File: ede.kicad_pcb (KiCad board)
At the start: 4 copper layers, 72.1 x 49 mm, 114 parts, among them J1 Conn_01x01, J10 Conn_01x01, J11 Conn_01x01, J12 Conn_01x01, J2 Conn_01x01, J3 Conn_01x01, J4 Conn_01x01, J5 Conn_01x06, J6 Conn_01x01, J7 Conn_01x04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

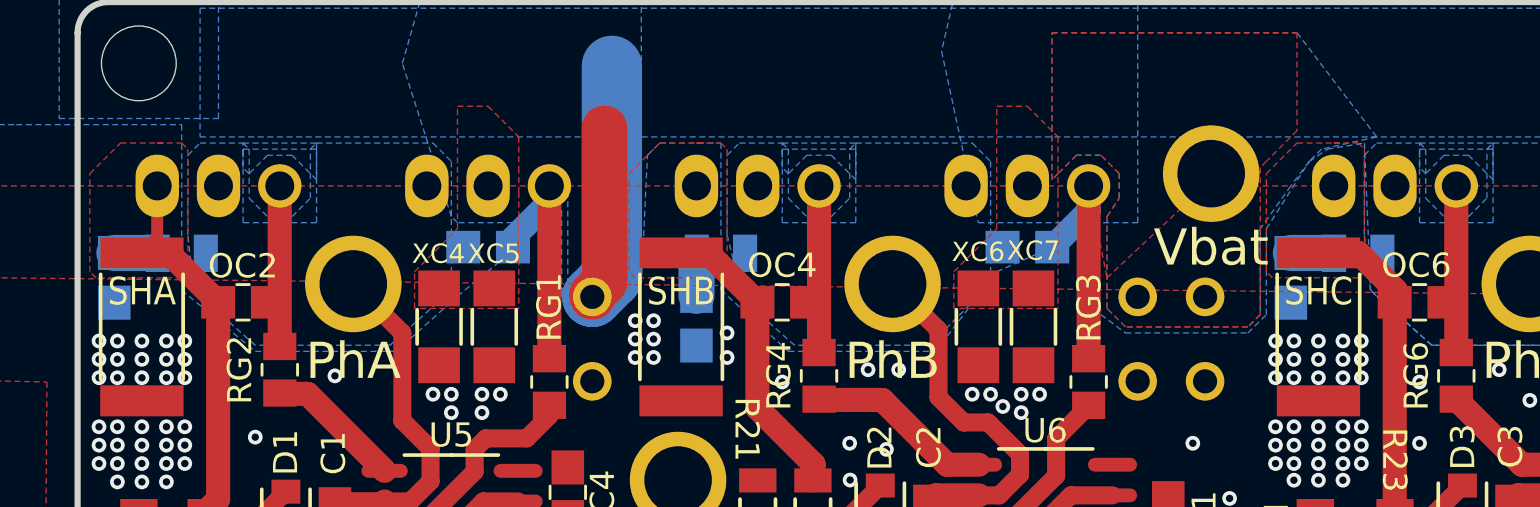
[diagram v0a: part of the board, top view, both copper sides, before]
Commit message: pcb: alter R0805 footprints on B.Cu as per reference
Signed-off-by: Afzal <afzal@intible.in>
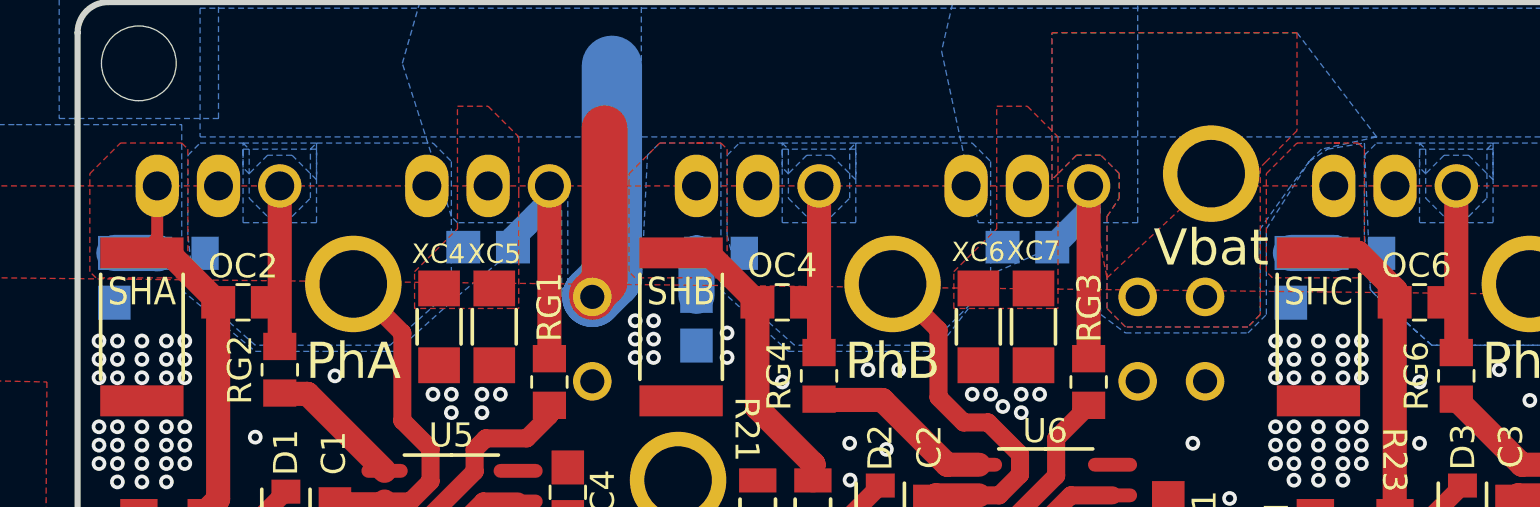
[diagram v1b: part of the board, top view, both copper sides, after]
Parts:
- RS1, RS2, RS3: footprint Intible:R_0805_2012Metric_EDE -> Intible:R_0805_2012Metric_small_EDE
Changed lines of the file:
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@@
     )
   )
-  (footprint "Intible:R_0805_2012Metric_EDE" locked (layer "B.Cu")
+  (footprint "Intible:R_0805_2012Metric_small_EDE" locked (layer "B.Cu")
     (at 97.5868 78.8416)
     (descr "Resistor SMD 0805 (2012 Metric), square (rectangular) end terminal, IPC_7351 nominal, (Body size source: IPC-SM-782 page 72, https://www.pcb-3d.com/wordpress/wp-content/uploads/ipc-sm-782a_amendment_1_and_2.pdf), generated with kicad-footprint-generator")
@@
     (property "exclude_from_bom" "")
     (attr smd exclude_from_bom)
-    (fp_text reference "RS3" (at 2.413 0.5334 90 unlocked) (layer "B.SilkS")
+    (fp_text reference "RS3" (at 2.413 0.5334 90) (layer "B.SilkS")
       (effects (font (size 1 1) (thickness 0.152)) (justify mirror))
     )
@@
       (effects (font (size 0.5 0.5) (thickness 0.08)) (justify mirror))
     )
-    (fp_line (start -0.227064 -0.735) (end 0.227064 -0.735) (layer "B.SilkS") (width 0.152))
-    (fp_line (start -0.227064 0.735) (end 0.227064 0.735) (layer "B.SilkS") (width 0.152))
-    (fp_line (start 1.68 0.95) (end 1.68 -0.95) (layer "B.CrtYd") (width 0.05))
+    (fp_line (start -0.227064 -0.735) (end 0.227064 -0.735) (layer "B.SilkS") (width 0.12))
+    (fp_line (start -0.227064 0.735) (end 0.227064 0.735) (layer "B.SilkS") (width 0.12))
     (fp_line (start -1.68 0.95) (end 1.68 0.95) (layer "B.CrtYd") (width 0.05))
     (fp_line (start 1.68 -0.95) (end -1.68 -0.95) (layer "B.CrtYd") (width 0.05))
     (fp_line (start -1.68 -0.95) (end -1.68 0.95) (layer "B.CrtYd") (width 0.05))
+    (fp_line (start 1.68 0.95) (end 1.68 -0.95) (layer "B.CrtYd") (width 0.05))
+    (fp_line (start 1 -0.625) (end -1 -0.625) (layer "B.Fab") (width 0.1))
+    (fp_line (start -1 -0.625) (end -1 0.625) (layer "B.Fab") (width 0.1))
+    (fp_line (start -1 0.625) (end 1 0.625) (layer "B.Fab") (width 0.1))
     (fp_line (start 1 0.625) (end 1 -0.625) (layer "B.Fab") (width 0.1))
-    (fp_line (start -1 -0.625) (end -1 0.625) (layer "B.Fab") (width 0.1))
-    (fp_line (start 1 -0.625) (end -1 -0.625) (layer "B.Fab") (width 0.1))
-    (fp_line (start -1 0.625) (end 1 0.625) (layer "B.Fab") (width 0.1))
-    (pad "1" smd rect locked (at -1 0) (size 1 1.55) (layers "B.Cu" "B.Paste" "B.Mask")
+    (pad "1" smd rect locked (at -0.9665 0) (size 1.133 1.377) (layers "B.Cu" "B.Paste" "B.Mask")
       (net 12 "Net-(CS3-Pad1)") (pintype "passive"))
-    (pad "2" smd rect locked (at 1 0) (size 1 1.55) (layers "B.Cu" "B.Paste" "B.Mask")
+    (pad "2" smd rect locked (at 0.9665 0) (size 1.133 1.377) (layers "B.Cu" "B.Paste" "B.Mask")
       (net 10 "/PHASEC") (pintype "passive"))
     (model "${KICAD6_3DMODEL_DIR}/Resistor_SMD.3dshapes/R_0805_2012Metric.wrl"
@@
     )
   )
-  (footprint "Intible:R_0805_2012Metric_EDE" locked (layer "B.Cu")
+  (footprint "Intible:R_0805_2012Metric_small_EDE" locked (layer "B.Cu")
     (at 71.1708 78.8416)
     (descr "Resistor SMD 0805 (2012 Metric), square (rectangular) end terminal, IPC_7351 nominal, (Body size source: IPC-SM-782 page 72, https://www.pcb-3d.com/wordpress/wp-content/uploads/ipc-sm-782a_amendment_1_and_2.pdf), generated with kicad-footprint-generator")
@@
     (property "exclude_from_bom" "")
     (attr smd exclude_from_bom)
-    (fp_text reference "RS2" (at 2.3622 0.4064 90 unlocked) (layer "B.SilkS")
+    (fp_text reference "RS2" (at 2.3622 0.4064 90) (layer "B.SilkS")
       (effects (font (size 1 1) (thickness 0.152)) (justify mirror))
     )
@@
       (effects (font (size 0.5 0.5) (thickness 0.08)) (justify mirror))
     )
-    (fp_line (start -0.227064 0.735) (end 0.227064 0.735) (layer "B.SilkS") (width 0.152))
-    (fp_line (start -0.227064 -0.735) (end 0.227064 -0.735) (layer "B.SilkS") (width 0.152))
+    (fp_line (start -0.227064 0.735) (end 0.227064 0.735) (layer "B.SilkS") (width 0.12))
+    (fp_line (start -0.227064 -0.735) (end 0.227064 -0.735) (layer "B.SilkS") (width 0.12))
+    (fp_line (start -1.68 0.95) (end 1.68 0.95) (layer "B.CrtYd") (width 0.05))
     (fp_line (start -1.68 -0.95) (end -1.68 0.95) (layer "B.CrtYd") (width 0.05))
-    (fp_line (start -1.68 0.95) (end 1.68 0.95) (layer "B.CrtYd") (width 0.05))
     (fp_line (start 1.68 -0.95) (end -1.68 -0.95) (layer "B.CrtYd") (width 0.05))
     (fp_line (start 1.68 0.95) (end 1.68 -0.95) (layer "B.CrtYd") (width 0.05))
+    (fp_line (start -1 -0.625) (end -1 0.625) (layer "B.Fab") (width 0.1))
+    (fp_line (start 1 -0.625) (end -1 -0.625) (layer "B.Fab") (width 0.1))
+    (fp_line (start 1 0.625) (end 1 -0.625) (layer "B.Fab") (width 0.1))
     (fp_line (start -1 0.625) (end 1 0.625) (layer "B.Fab") (width 0.1))
-    (fp_line (start -1 -0.625) (end -1 0.625) (layer "B.Fab") (width 0.1))
-    (fp_line (start 1 0.625) (end 1 -0.625) (layer "B.Fab") (width 0.1))
-    (fp_line (start 1 -0.625) (end -1 -0.625) (layer "B.Fab") (width 0.1))
-    (pad "1" smd rect locked (at -1 0) (size 1 1.55) (layers "B.Cu" "B.Paste" "B.Mask")
+    (pad "1" smd rect locked (at -0.9665 0) (size 1.133 1.377) (layers "B.Cu" "B.Paste" "B.Mask")
       (net 11 "Net-(CS2-Pad1)") (pintype "passive"))
-    (pad "2" smd rect locked (at 1 0) (size 1 1.55) (layers "B.Cu" "B.Paste" "B.Mask")
+    (pad "2" smd rect locked (at 0.9665 0) (size 1.133 1.377) (layers "B.Cu" "B.Paste" "B.Mask")
       (net 3 "/PHASEB") (pintype "passive"))
     (model "${KICAD6_3DMODEL_DIR}/Resistor_SMD.3dshapes/R_0805_2012Metric.wrl"
@@
     )
   )
-  (footprint "Intible:R_0805_2012Metric_EDE" locked (layer "B.Cu")
+  (footprint "Intible:R_0805_2012Metric_small_EDE" locked (layer "B.Cu")
     (at 48.8188 78.8416)
     (descr "Resistor SMD 0805 (2012 Metric), square (rectangular) end terminal, IPC_7351 nominal, (Body size source: IPC-SM-782 page 72, https://www.pcb-3d.com/wordpress/wp-content/uploads/ipc-sm-782a_amendment_1_and_2.pdf), generated with kicad-footprint-generator")
@@
     (property "exclude_from_bom" "")
     (attr smd exclude_from_bom)
-    (fp_text reference "RS1" (at -0.8128 2.413 90 unlocked) (layer "B.SilkS")
+    (fp_text reference "RS1" (at -0.8128 2.413 90) (layer "B.SilkS")
       (effects (font (size 1 1) (thickness 0.152)) (justify mirror))
     )
@@
       (effects (font (size 0.5 0.5) (thickness 0.08)) (justify mirror))
     )
-    (fp_line (start -0.227064 -0.735) (end 0.227064 -0.735) (layer "B.SilkS") (width 0.152))
-    (fp_line (start -0.227064 0.735) (end 0.227064 0.735) (layer "B.SilkS") (width 0.152))
+    (fp_line (start -0.227064 -0.735) (end 0.227064 -0.735) (layer "B.SilkS") (width 0.12))
+    (fp_line (start -0.227064 0.735) (end 0.227064 0.735) (layer "B.SilkS") (width 0.12))
+    (fp_line (start -1.68 -0.95) (end -1.68 0.95) (layer "B.CrtYd") (width 0.05))
+    (fp_line (start -1.68 0.95) (end 1.68 0.95) (layer "B.CrtYd") (width 0.05))
     (fp_line (start 1.68 0.95) (end 1.68 -0.95) (layer "B.CrtYd") (width 0.05))
-    (fp_line (start -1.68 0.95) (end 1.68 0.95) (layer "B.CrtYd") (width 0.05))
     (fp_line (start 1.68 -0.95) (end -1.68 -0.95) (layer "B.CrtYd") (width 0.05))
-    (fp_line (start -1.68 -0.95) (end -1.68 0.95) (layer "B.CrtYd") (width 0.05))
+    (fp_line (start 1 -0.625) (end -1 -0.625) (layer "B.Fab") (width 0.1))
     (fp_line (start 1 0.625) (end 1 -0.625) (layer "B.Fab") (width 0.1))
-    (fp_line (start 1 -0.625) (end -1 -0.625) (layer "B.Fab") (width 0.1))
     (fp_line (start -1 -0.625) (end -1 0.625) (layer "B.Fab") (width 0.1))
     (fp_line (start -1 0.625) (end 1 0.625) (layer "B.Fab") (width 0.1))
-    (pad "1" smd rect locked (at -1 0) (size 1 1.55) (layers "B.Cu" "B.Paste" "B.Mask")
+    (pad "1" smd rect locked (at -0.9665 0) (size 1.133 1.377) (layers "B.Cu" "B.Paste" "B.Mask")
       (net 5 "Net-(CS1-Pad1)") (pintype "passive"))
-    (pad "2" smd rect locked (at 1 0) (size 1 1.55) (layers "B.Cu" "B.Paste" "B.Mask")
+    (pad "2" smd rect locked (at 0.9665 0) (size 1.133 1.377) (layers "B.Cu" "B.Paste" "B.Mask")
       (net 2 "/PHASEA") (pintype "passive"))
     (model "${KICAD6_3DMODEL_DIR}/Resistor_SMD.3dshapes/R_0805_2012Metric.wrl"

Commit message: pcb: bring In2.Cu +12V busbar more similar to v0.5.2
Signed-off-by: Afzal <afzal@intible.in>
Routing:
- net +12V: track 127.7 -> 127.2 mm
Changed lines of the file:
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@@
   (via (at 90.7288 91.5416) (size 0.61) (drill 0.305) (layers "F.Cu" "B.Cu") (net 1))
   (via (at 76.5048 91.5416) (size 0.61) (drill 0.305) (layers "F.Cu" "B.Cu") (net 1))
+  (segment (start 111.3282 90.932) (end 112.5518 92.1556) (width 1.5) (layer "In2.Cu") (net 1))
   (segment (start 112.5518 92.5576) (end 113.5888 92.5576) (width 1.5) (layer "In2.Cu") (net 1))
   (segment (start 90.7288 91.5416) (end 88.6968 91.5416) (width 1.5) (layer "In2.Cu") (net 1))
+  (segment (start 101.7524 90.932) (end 111.3282 90.932) (width 1.5) (layer "In2.Cu") (net 1))
+  (segment (start 112.5518 92.1556) (end 112.5518 92.5576) (width 1.5) (layer "In2.Cu") (net 1))
   (segment (start 63.225756 91.5416) (end 76.5048 91.5416) (width 1.5) (layer "In2.Cu") (net 1))
   (segment (start 91.2368 92.0496) (end 90.7288 91.5416) (width 1.5) (layer "In2.Cu") (net 1))
   (segment (start 78.8162 89.2302) (end 78.8162 89.1794) (width 1.5) (layer "In2.Cu") (net 1))
-  (segment (start 102.1588 90.5256) (end 100.6348 92.0496) (width 1.5) (layer "In2.Cu") (net 1))
+  (segment (start 100.6348 92.0496) (end 101.7524 90.932) (width 1.5) (layer "In2.Cu") (net 1))
   (segment (start 61.7474 104.0638) (end 59.7408 102.0572) (width 1.5) (layer "In2.Cu") (net 1))
-  (segment (start 112.5518 92.5576) (end 112.5518 91.842) (width 1.5) (layer "In2.Cu") (net 1))
   (segment (start 76.5048 91.5416) (end 78.8162 89.2302) (width 1.5) (layer "In2.Cu") (net 1))
   (segment (start 59.7408 95.026556) (end 63.225756 91.5416) (width 1.5) (layer "In2.Cu") (net 1))
   (segment (start 86.3346 89.1794) (end 88.6968 91.5416) (width 1.5) (layer "In2.Cu") (net 1))
   (segment (start 63.0428 114.1476) (end 61.7982 112.903) (width 1.5) (layer "In2.Cu") (net 1))
-  (segment (start 111.379 90.5256) (end 102.1588 90.5256) (width 1.5) (layer "In2.Cu") (net 1))
-  (segment (start 112.5982 91.7448) (end 111.379 90.5256) (width 1.5) (layer "In2.Cu") (net 1))
   (segment (start 78.8162 89.1794) (end 86.3346 89.1794) (width 1.5) (layer "In2.Cu") (net 1))
   (segment (start 100.6348 92.0496) (end 91.2368 92.0496) (width 1.5) (layer "In2.Cu") (net 1))
